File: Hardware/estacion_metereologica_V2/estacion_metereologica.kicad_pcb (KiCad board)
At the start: 2 copper layers, 21 parts, among them J1 Screw_Terminal_01x02, J2 Step_Down_Mini, J3 Conn_01x03_Pin

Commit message: Segunda version del PCB
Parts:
- added C_0.33µF3: C, Capacitor_SMD:C_0805_2012Metric, B.Cu at (58.4, 77.5)
- added C_0.33µF4: C, Capacitor_SMD:C_0805_2012Metric, B.Cu at (58.4, 81.7)
- added U1: AMS1117, Package_TO_SOT_SMD:SOT-223-3_TabPin2, B.Cu at (65.2, 80.7)
- moved J3 13.2 mm to (33.0, 84.7), turned to 180 degrees
- moved J1 10.7 mm to (29.6, 71.9), turned to -90 degrees
- moved C_0.33µF1 9.69 mm to (47.7, 75.9)
- moved C_0.33µF2 9.69 mm to (44.0, 75.9)
- moved J2 9.69 mm to (36.9, 86.6)
- moved R6 8.84 mm to (61.4, 33.0), turned to -90 degrees
- moved R5 8.57 mm to (69.8, 33.0), turned to -90 degrees
- moved R2 6.20 mm to (72.4, 45.3)
- moved R1 6.19 mm to (72.4, 73.0)
- moved R3 6.19 mm to (72.4, 54.5)
- moved R4 6.19 mm to (72.4, 61.6)
- moved hall_1_este1 4.12 mm to (80.6, 68.0)
- moved hall_1_oeste1 4.12 mm to (80.6, 49.5)
- moved hall_2_oeste1 4.12 mm to (80.6, 58.6)
- moved hall_2_sur1 4.12 mm to (80.6, 40.3)
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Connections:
- Esp1 pad 1: 3V3 -> unconnected-(Esp1-3V3-Pad1)
- Esp1 pad 10: OUT_1 -> unconnected-(Esp1-IO26-Pad10)
- Esp1 pad 11: OUT_2 -> unconnected-(Esp1-IO27-Pad11)
- Esp1 pad 12: OUT_3 -> unconnected-(Esp1-IO14-Pad12)
- Esp1 pad 15: OUT_4 -> unconnected-(Esp1-IO13-Pad15)
- Esp1 pad 30: unconnected-(Esp1-IO18-Pad30) -> OUT_2
- Esp1 pad 31: unconnected-(Esp1-IO19-Pad31) -> OUT_3
- Esp1 pad 7: unconnected-(Esp1-IO32-Pad7) -> OUT_4
- Esp1 pad 8: unconnected-(Esp1-IO33-Pad8) -> OUT_1
- J3 pad 2: unconnected-(J3-Pin_2-Pad2) -> Net-(J1-Pin_2)
- J3 pad 3: Net-(J1-Pin_2) -> unconnected-(J3-Pin_3-Pad3)
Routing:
- net 3V3: track 238.8 -> 175.2 mm, vias 6 -> 8
- net VO+: track 187.6 -> 142.9 mm
- net OUT_2: track 52.7 -> 35.5 mm
- net OUT_4: track 24.5 -> 40.6 mm
- net OUT_6: track 20.2 -> 14.4 mm
- net OUT_3: track 41.1 -> 46.7 mm
- net OUT_5: track 26.7 -> 21.6 mm
- net VIN+: track 11.8 -> 16.0 mm
- net SCL: track 27.9 -> 25.1 mm
- net Net-(J1-Pin_2): track 10.0 -> 8.28 mm
- net OUT_1: track 38.8 -> 39.9 mm
- net SDA: track 18.8 -> 19.9 mm
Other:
- board outline added: 62.7 x 61.9 mm

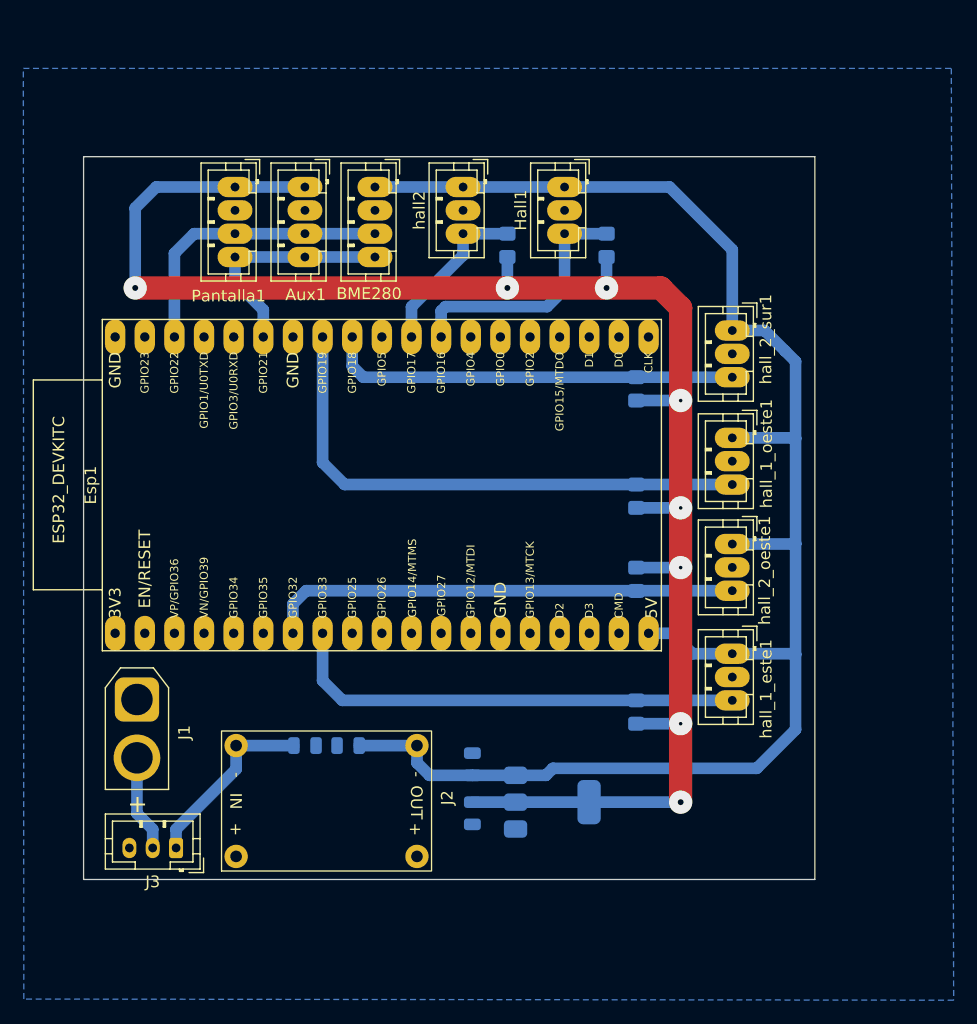
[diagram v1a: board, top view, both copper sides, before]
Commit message: se actualizo detalles del PCB
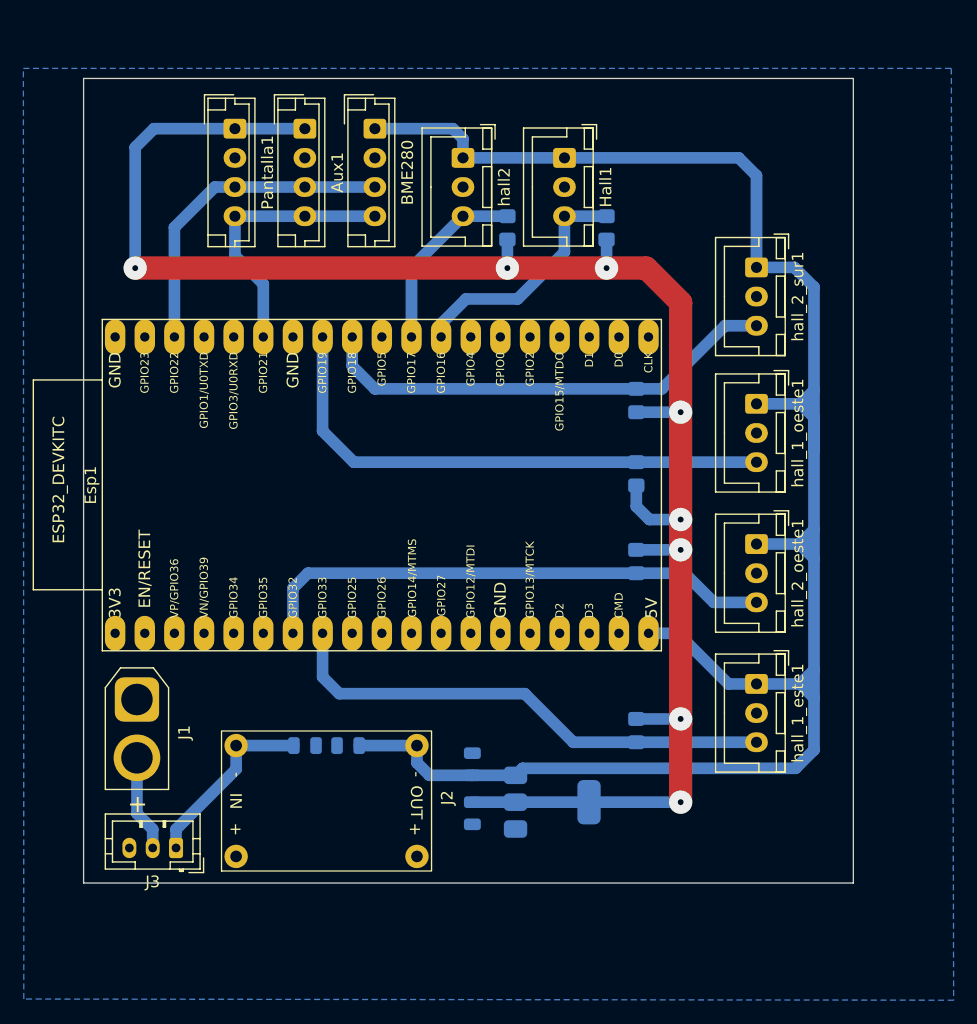
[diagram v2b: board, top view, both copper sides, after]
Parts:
- Aux1, BME280, Pantalla1: footprint Connector_JST:JST_PH_B4B-PH-K_1x04_P2.00mm_Vertical -> Connector_JST:JST_EH_B4B-EH-A_1x04_P2.50mm_Vertical
- Hall1, hall2, hall_1_este1, hall_1_oeste1, hall_2_oeste1, hall_2_sur1: footprint Connector_JST:JST_PH_B3B-PH-K_1x03_P2.00mm_Vertical -> Connector_JST:JST_XH_B3B-XH-A_1x03_P2.50mm_Vertical
- moved hall_2_sur1 5.80 mm to (82.7, 34.9)
- moved Aux1 5.00 mm to (44.0, 23.0)
- moved BME280 5.00 mm to (50.0, 23.0)
- moved Pantalla1 5.00 mm to (38.0, 23.0)
- moved hall_1_oeste1 3.58 mm to (82.7, 46.6)
- moved hall_1_este1 3.32 mm to (82.7, 70.6)
- moved Hall1 2.50 mm to (66.2, 25.5)
- moved hall2 2.50 mm to (57.5, 25.5)
- moved hall_2_oeste1 2.08 mm to (82.7, 58.6)
- moved R3 1.92 mm to (72.4, 52.6)
- moved R1 1.59 mm to (72.4, 74.6), turned to 90 degrees
- moved R4 1.52 mm to (72.4, 60.1)
- moved R5 1.50 mm to (69.8, 31.5)
- moved R6 1.50 mm to (61.4, 31.5)
- moved R2 1.00 mm to (72.4, 46.3)
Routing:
- net VO+: track 142.9 -> 165.4 mm
- net 3V3: track 175.2 -> 181.5 mm
- net OUT_2: track 35.5 -> 40.2 mm
- net OUT_4: track 40.6 -> 45.2 mm
- net SDA: track 19.9 -> 23.4 mm
- net OUT_1: track 39.9 -> 43.3 mm
- net SCL: track 25.1 -> 28.0 mm
- net OUT_6: track 14.4 -> 16.0 mm
- net OUT_5: track 21.6 -> 20.9 mm
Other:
- board size 62.7 x 61.9 mm -> 66 x 69 mm

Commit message: se actualizo detalles del PCB
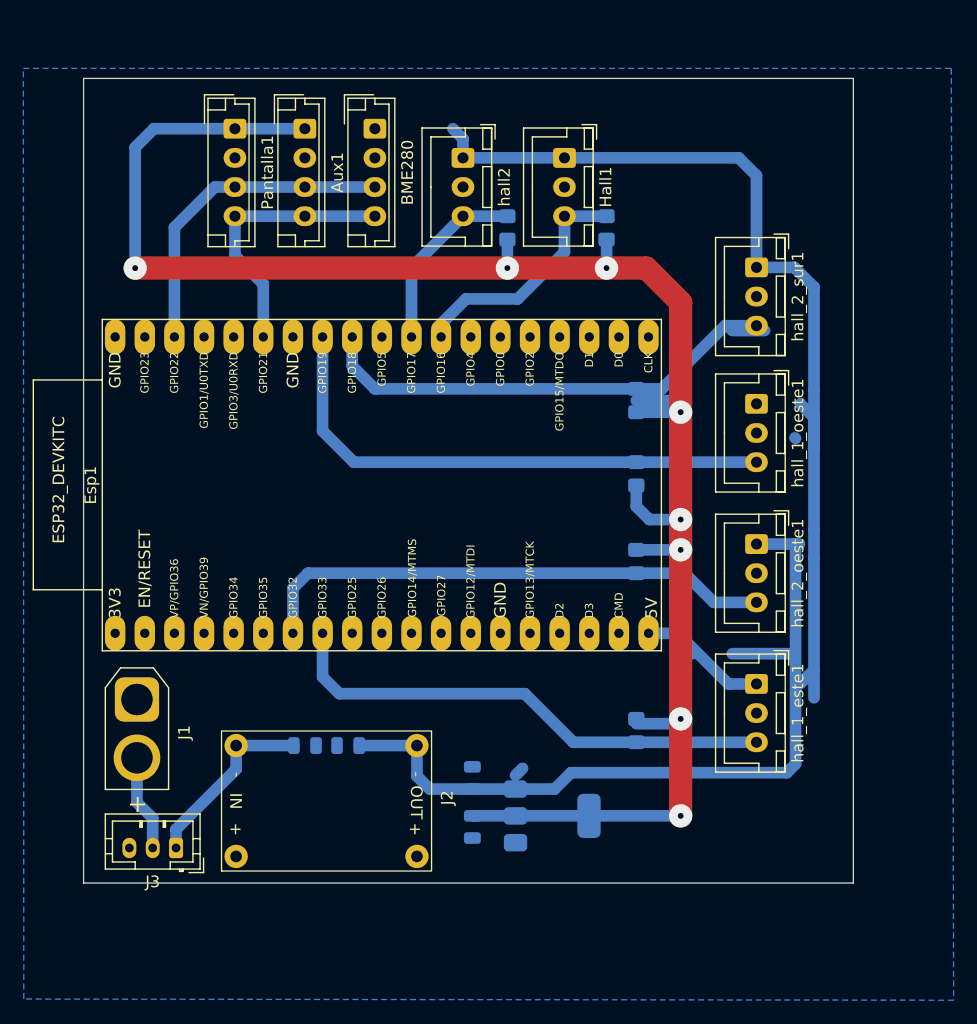
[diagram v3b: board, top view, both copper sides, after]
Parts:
- moved C_0.33µF3 1.18 mm to (58.4, 78.7)
- moved U1 1.18 mm to (65.2, 81.9)
- moved C_0.33µF4 1.17 mm to (58.4, 82.8)
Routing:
- net 3V3: track 181.5 -> 186.5 mm
- net VO+: track 165.4 -> 169.9 mm
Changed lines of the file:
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@@
 	(footprint "Package_TO_SOT_SMD:SOT-223-3_TabPin2"
 		(layer "B.Cu")
-		(at 65.2 80.725)
+		(at 65.2 81.9)
 		(descr "module CMS SOT223 4 pins")
 		(tags "CMS SOT")
@@
 	(footprint "Capacitor_SMD:C_0805_2012Metric"
 		(layer "B.Cu")
-		(at 58.35 77.475 90)
+		(at 58.35 78.65 90)
 		(descr "Capacitor SMD 0805 (2012 Metric), square (rectangular) end terminal, IPC_7351 nominal, (Body size source: IPC-SM-782 page 76, https://www.pcb-3d.com/wordpress/wp-content/uploads/ipc-sm-782a_amendment_1_and_2.pdf, https://docs.google.com/spreadsheets/d/1BsfQQcO9C6DZCsRaXUlFlo91Tg2WpOkGARC1WS5S8t0/edit?usp=sharing), generated with kicad-footprint-generator")
 		(tags "capacitor")
@@
 	(footprint "Capacitor_SMD:C_0805_2012Metric"
 		(layer "B.Cu")
-		(at 58.35 81.675 -90)
+		(at 58.35 82.85 -90)
 		(descr "Capacitor SMD 0805 (2012 Metric), square (rectangular) end terminal, IPC_7351 nominal, (Body size source: IPC-SM-782 page 76, https://www.pcb-3d.com/wordpress/wp-content/uploads/ipc-sm-782a_amendment_1_and_2.pdf, https://docs.google.com/spreadsheets/d/1BsfQQcO9C6DZCsRaXUlFlo91Tg2WpOkGARC1WS5S8t0/edit?usp=sharing), generated with kicad-footprint-generator")
 		(tags "capacitor")
@@
 	)
 	(segment
-		(start 76.2 80.725)
+		(start 76.2 81.9)
 		(end 76.2 74)
 		(width 2)
@@
 	)
 	(via
-		(at 76.2 80.725)
+		(at 76.2 81.9)
 		(size 2)
 		(drill 0.5)
@@
 	)
 	(segment
-		(start 76.2 73.5904)
-		(end 72.4 73.5904)
+		(start 68.35 81.9)
+		(end 76.2 81.9)
+		(width 1)
+		(layer "B.Cu")
+		(net 2)
+	)
+	(segment
+		(start 72.4 74)
+		(end 76.2 74)
 		(width 1)
 		(layer "B.Cu")
@@
 	)
 	(segment
-		(start 68.35 80.725)
-		(end 62.05 80.725)
-		(width 1)
-		(layer "B.Cu")
-		(net 2)
-	)
-	(segment
-		(start 68.35 80.725)
-		(end 76.2 80.725)
-		(width 1)
-		(layer "B.Cu")
-		(net 2)
-	)
-	(segment
-		(start 62.05 80.725)
-		(end 58.35 80.725)
+		(start 68.35 81.9)
+		(end 62.05 81.9)
+		(width 1)
+		(layer "B.Cu")
+		(net 2)
+	)
+	(segment
+		(start 72.4 46.3)
+		(end 76.2 46.3)
+		(width 1)
+		(layer "B.Cu")
+		(net 2)
+	)
+	(segment
+		(start 62.05 81.9)
+		(end 58.35 81.9)
 		(width 1)
 		(layer "B.Cu")
@@
 	)
 	(segment
-		(start 30.95 83.05)
-		(end 29.6 81.7)
+		(start 29.6 80.75)
+		(end 29.6 76.925)
 		(width 1)
 		(layer "B.Cu")
@@
 	)
 	(segment
-		(start 29.6 81.7)
-		(end 29.6 76.925)
+		(start 30.95 82.1)
+		(end 29.6 80.75)
 		(width 1)
 		(layer "B.Cu")
@@
 	(segment
 		(start 30.95 84.65)
-		(end 30.95 83.05)
+		(end 30.95 82.1)
 		(width 1)
 		(layer "B.Cu")
@@
 	)
 	(segment
-		(start 86.4616 46.5836)
-		(end 82.7024 46.5836)
-		(width 1)
-		(layer "B.Cu")
-		(net 36)
-	)
-	(segment
-		(start 53.6 77.35)
-		(end 54.675 78.425)
-		(width 1)
-		(layer "B.Cu")
-		(net 36)
-	)
-	(segment
-		(start 53.6 75.875)
-		(end 53.6 77.35)
+		(start 53.6 78.5)
+		(end 54.7 79.6)
 		(width 1)
 		(layer "B.Cu")
@@
 	)
 	(segment
-		(start 86.0568 77.824)
-		(end 87.63 76.2508)
-		(width 1)
-		(layer "B.Cu")
-		(net 36)
-	)
-	(segment
-		(start 87.63 59.8424)
-		(end 86.3876 58.6)
-		(width 1)
-		(layer "B.Cu")
-		(net 36)
-	)
-	(segment
-		(start 86.44 70.5904)
-		(end 87.63 71.7804)
-		(width 1)
-		(layer "B.Cu")
-		(net 36)
-	)
-	(segment
-		(start 86.3876 58.6)
-		(end 86.3876 58.5956)
-		(width 1)
-		(layer "B.Cu")
-		(net 36)
-	)
-	(segment
-		(start 62.651 77.824)
-		(end 86.0568 77.824)
-		(width 1)
-		(layer "B.Cu")
-		(net 36)
-	)
-	(segment
-		(start 86.3876 58.5956)
-		(end 87.63 57.3532)
+		(start 86.025 58.6)
+		(end 86.05 58.575)
+		(width 1)
+		(layer "B.Cu")
+		(net 36)
+	)
+	(segment
+		(start 53.6 75.875)
+		(end 53.6 78.5)
+		(width 1)
+		(layer "B.Cu")
+		(net 36)
+	)
+	(segment
+		(start 85.3 78.2)
+		(end 85.55 77.95)
+		(width 1)
+		(layer "B.Cu")
+		(net 36)
+	)
+	(segment
+		(start 62.05 79.6)
+		(end 65.4 79.6)
+		(width 1)
+		(layer "B.Cu")
+		(net 36)
+	)
+	(segment
+		(start 80.625 68)
+		(end 86 68)
+		(width 1)
+		(layer "B.Cu")
+		(net 36)
+	)
+	(segment
+		(start 86 49.5)
+		(end 86.05 49.55)
 		(width 1)
 		(layer "B.Cu")
@@
 	)
 	(segment
+		(start 54.7 79.6)
+		(end 58.35 79.6)
+		(width 1)
+		(layer "B.Cu")
+		(net 36)
+	)
+	(segment
 		(start 48.65 75.875)
 		(end 53.45 75.875)
@@
 	)
 	(segment
-		(start 87.63 76.2508)
-		(end 87.63 71.7804)
+		(start 85.55 77.95)
+		(end 86.05 77.45)
 		(width 1)
 		(layer "B.Cu")
@@
 	)
 	(segment
-		(start 86.44 70.5904)
-		(end 86.44 70.5828)
+		(start 66.8 78.2)
+		(end 85.3 78.2)
+		(width 1)
+		(layer "B.Cu")
+		(net 36)
+	)
+	(segment
+		(start 86.05 77.45)
+		(end 86.05 58.575)
+		(width 1)
+		(layer "B.Cu")
+		(net 36)
+	)
+	(segment
+		(start 80.625 40.3)
+		(end 83.4 40.3)
 		(width 1)
 		(layer "B.Cu")
@@
 	)
 	(segment
-		(start 62.05 78.425)
-		(end 58.35 78.425)
-		(width 1)
-		(layer "B.Cu")
-		(net 36)
-	)
-	(segment
-		(start 82.7024 70.5904)
-		(end 86.44 70.5904)
+		(start 58.35 79.6)
+		(end 62.05 79.6)
 		(width 1)
 		(layer "B.Cu")
@@
 	)
 	(segment
-		(start 49.9932 23.0016)
-		(end 56.682 23.0016)
-		(width 1)
-		(layer "B.Cu")
-		(net 36)
-	)
-	(segment
-		(start 86.4616 46.5836)
-		(end 87.63 45.4152)
+		(start 75.475 66.25)
+		(end 77.225 68)
 		(width 1)
 		(layer "B.Cu")
@@
 	)
 	(segment
-		(start 54.675 78.425)
-		(end 58.35 78.425)
-		(width 1)
-		(layer "B.Cu")
+		(start 65.4 79.6)
+		(end 66.8 78.2)
+		(width 1)
+		(layer "B.Cu")

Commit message: Se actualizo detalles del PCB
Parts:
- moved BME280 2.42 mm to (48.8, 25.1)
- moved Pantalla1 2.42 mm to (36.8, 25.1)
- moved Aux1 2.42 mm to (42.8, 25.1)
- moved C_0.33µF4 1.70 mm to (58.3, 84.5)
- moved C_0.33µF3 1.70 mm to (58.3, 80.3)
- moved U1 1.70 mm to (65.2, 83.6)
- moved Hall1 0.45 mm to (66.2, 25.1)
- moved R5 0.45 mm to (69.8, 31.1)
- moved R6 0.45 mm to (61.4, 31.1)
- moved hall2 0.45 mm to (57.5, 25.1)
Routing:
- net 3V3: track 186.5 -> 159.5 mm
- net SCL: track 28.0 -> 25.4 mm
- net OUT_6: track 16.0 -> 18.4 mm
- net OUT_5: track 20.9 -> 23.3 mm
- net SDA: track 23.4 -> 21.2 mm
- net VO+: track 169.9 -> 171.1 mm
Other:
- board size 66 x 69 mm -> 64.8 x 67.2 mm

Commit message: Version v3 del PCB
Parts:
- removed C_0.33µF1, C_0.33µF2: C, Capacitor_SMD:C_0805_2012Metric
- AMS1117: renamed from U1; value AMS1117 -> Regulador 3V3
- BME280: value Conn_01x04_Pin -> Conn_01x06_Pin; footprint Connector_JST:JST_EH_B4B-EH-A_1x04_P2.50mm_Vertical -> Connector_PinHeader_2.54mm:PinHeader_1x06_P2.54mm_Vertical
- Mini360: renamed from J2; value Step_Down_Mini -> Regulador 5V
- moved Pantalla1 6.30 mm to (35.3, 19.0)
- moved BME280 6.25 mm to (48.0, 18.9), turned to 0 degrees
- moved Aux1 6.12 mm to (42.9, 19.0)
- moved Hall1 2.44 mm to (68.7, 25.0)
- moved R5 2.44 mm to (72.3, 31.0)
- moved R6 2.44 mm to (63.8, 31.0)
- moved hall2 2.44 mm to (60.0, 25.0)
- moved Switch1 0.17 mm to (32.9, 84.5)
- renumbered Esp1 to Esp32, J3 to Switch1, J1 to XT30
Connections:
- BME280 pad 1: VO+ -> 3V3
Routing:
- net 3V3: track 159.5 -> 188.8 mm
- net VO+: track 171.1 -> 152.1 mm
- net SDA: track 21.2 -> 30.6 mm
- net SCL: track 25.4 -> 31.6 mm
- net VIN+: track 16.0 -> 10.8 mm
- net OUT_5: track 23.3 -> 26.2 mm
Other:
- board size 64.8 x 67.2 mm -> 64.8 x 74.9 mm
